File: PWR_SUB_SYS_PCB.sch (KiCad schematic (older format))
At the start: 0 parts

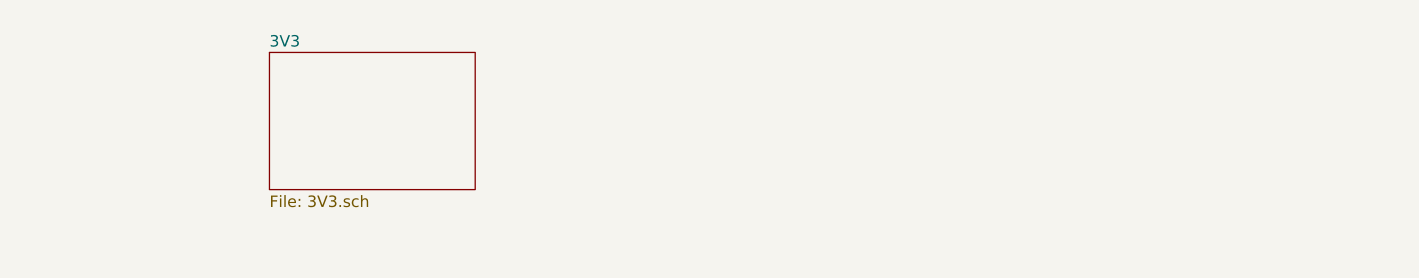
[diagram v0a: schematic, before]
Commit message: added data logging
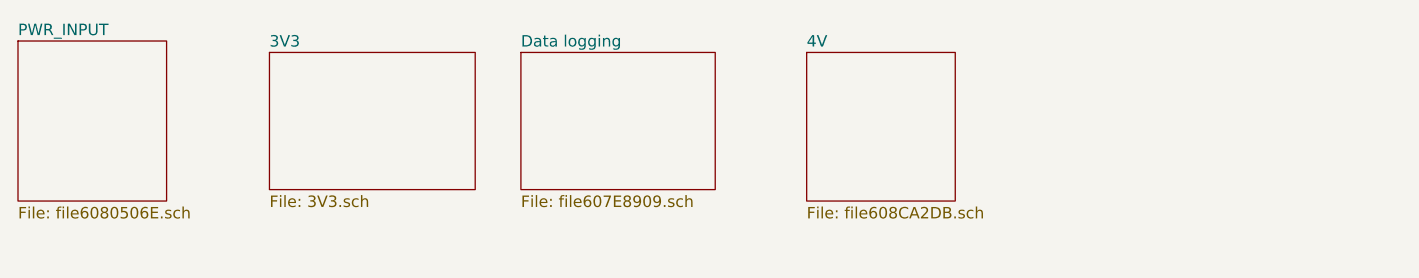
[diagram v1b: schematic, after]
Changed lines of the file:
@@
 $Descr A4 11693 8268
 encoding utf-8
-Sheet 1 5
+Sheet 1 10
 Title ""
 Date ""
@@
 F1 "3V3.sch" 50
 $EndSheet
+$Sheet
+S 3650 1450 850  600
+U 607E890A
+F0 "Data logging" 50
+F1 "file607E8909.sch" 50
+$EndSheet
+$Sheet
+S 1450 1400 650  700
+U 6080506F
+F0 "PWR_INPUT" 50
+F1 "file6080506E.sch" 50
+$EndSheet
+$Sheet
+S 4900 1450 650  650
+U 608CA2DC
+F0 "4V" 50
+F1 "file608CA2DB.sch" 50
+$EndSheet
 $EndSCHEMATC

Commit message: full schematic, version 1.0
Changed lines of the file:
@@
 $Descr A4 11693 8268
 encoding utf-8
-Sheet 1 10
+Sheet 1 15
 Title ""
 Date ""
@@
 F1 "file608CA2DB.sch" 50
 $EndSheet
+$Sheet
+S 6400 1450 1100 800
+U 60925CA4
+F0 "12V" 50
+F1 "file60925CA3.sch" 50
+$EndSheet
 $EndSCHEMATC
